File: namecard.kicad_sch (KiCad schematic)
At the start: 25 parts, among them J1 Conn_01x24, J2 Conn_01x05, Q1 AO3400A, U1 STM32G030K6Tx, U2 ST25DV04K-IER8C3

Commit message: 電源回路周りの調整
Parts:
- added C13, C8: 0.1uF, Capacitor_SMD:C_0603_1608Metric, symbol Device:C
- added D4: D_Schottky, symbol Device:D_Schottky
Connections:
- net +3.3V is gone; now on net EXT_3V3: C1.1, C4.1, L1.2
- net SYS_VDD is gone; now on net EXT_3V3: U1.4 (VDD)
- net EXT_3V3: now also U2.8 (VCC), C8.1, D4.1 (K)
- net GND: now also C13.2, C8.2
- net NRST: now also C13.1
- net V_EH_RAW: now also C_Tank1.1, D4.2 (A)

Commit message: 基盤配置の調整
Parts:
- removed C_Tank1: 330uF, Capacitor_Tantalum_SMD:CP_EIA-3216-18_Kemet-A, symbol Device:C
- added C14, C15, C16, C17, C18, C19, C20, C21, C22, C23: 22uf, Capacitor_SMD:C_0805_2012Metric, symbol Device:C
- D4: footprint (none) -> Diode_SMD:D_SOD-123
- J1: footprint Connector_FFC-FPC:Hirose_FH12-24S-0.5SH_1x24-1MP_P0.50mm_Horizontal -> FH34SRJ-24S-0.5SH(50)
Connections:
- net GND: now also C14.2, C15.2, C16.2, C17.2, C18.2, C19.2, C20.2, C21.2, C22.2, C23.2
- net V_EH_RAW: now also C14.1, C15.1, C16.1, C17.1, C18.1, C19.1, C20.1, C21.1, C22.1, C23.1

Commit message: v2 production
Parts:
- C14, C15, C16, C17, C18, C19, C20, C21, C22, C23: LCSC (none) -> C45783
- D4: LCSC (none) -> C22374920
- J1: footprint FH34SRJ-24S-0.5SH(50) -> Connector:FFC-SMD_24P-P0.50_FH34SRJ-24S-0.5SH; LCSC (none) -> C324726
- L1: LCSC (none) -> C66936
- U1: LCSC (none) -> C529331
- U2: LCSC (none) -> C2908287
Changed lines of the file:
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@@
 			)
 		)
+		(property "LCSC" "C45783"
+			(at 0 0 0)
+			(show_name no)
+			(do_not_autoplace no)
+			(effects
+				(font
+					(size 1.27 1.27)
+				)
+			)
+		)
 		(pin "1"
 		)
@@
 			)
 		)
+		(property "LCSC" "C22374920"
+			(at 35.56 66.04 0)
+			(hide yes)
+			(show_name no)
+			(do_not_autoplace no)
+			(effects
+				(font
+					(size 1.27 1.27)
+				)
+			)
+		)
 		(pin "1"
 		)
@@
 			)
 		)
+		(property "LCSC" "C66936"
+			(at 127 74.93 0)
+			(hide yes)
+			(show_name no)
+			(do_not_autoplace no)
+			(effects
+				(font
+					(size 1.27 1.27)
+				)
+			)
+		)
 		(pin "1"
 		)
@@
 			)
 		)
+		(property "LCSC" "C45783"
+			(at 0 0 0)
+			(show_name no)
+			(do_not_autoplace no)
+			(effects
+				(font
+					(size 1.27 1.27)
+				)
+			)
+		)
 		(pin "1"
 		)
@@
 			)
 		)
+		(property "LCSC" "C2908287"
+			(at 104.14 124.46 0)
+			(hide yes)
+			(show_name no)
+			(do_not_autoplace no)
+			(effects
+				(font
+					(size 1.27 1.27)
+				)
+			)
+		)
 		(pin "5"
 		)
@@
 			)
 		)
+		(property "LCSC" "C529331"
+			(at 44.45 115.57 0)
+			(hide yes)
+			(show_name no)
+			(do_not_autoplace no)
+			(effects
+				(font
+					(size 1.27 1.27)
+				)
+			)
+		)
 		(pin "20"
 		)
@@
 			)
 		)
+		(property "LCSC" "C45783"
+			(at 0 0 0)
+			(show_name no)
+			(do_not_autoplace no)
+			(effects
+				(font
+					(size 1.27 1.27)
+				)
+			)
+		)
 		(pin "1"
 		)
@@
 			)
 		)
+		(property "LCSC" "C45783"
+			(at 0 0 0)
+			(show_name no)
+			(do_not_autoplace no)
+			(effects
+				(font
+					(size 1.27 1.27)
+				)
+			)
+		)
 		(pin "1"
 		)
@@
 			)
 		)
+		(property "LCSC" "C45783"
+			(at 81.28 53.34 0)
+			(hide yes)
+			(show_name no)
+			(do_not_autoplace no)
+			(effects
+				(font
+					(size 1.27 1.27)
+				)
+			)
+		)
 		(pin "1"
 		)
@@
 			)
 		)
+		(property "LCSC" "C45783"
+			(at 0 0 0)
+			(show_name no)
+			(do_not_autoplace no)
+			(effects
+				(font
+					(size 1.27 1.27)
+				)
+			)
+		)
 		(pin "1"
 		)
@@
 			)
 		)
+		(property "LCSC" "C45783"
+			(at 0 0 0)
+			(show_name no)
+			(do_not_autoplace no)
+			(effects
+				(font
+					(size 1.27 1.27)
+				)
+			)
+		)
 		(pin "1"
 		)
@@
 			)
 		)
+		(property "LCSC" "C45783"
+			(at 0 0 0)
+			(show_name no)
+			(do_not_autoplace no)
+			(effects
+				(font
+					(size 1.27 1.27)
+				)
+			)
+		)
 		(pin "1"
 		)
@@
 			)
 		)
-		(property "Footprint" "FH34SRJ-24S-0.5SH(50)"
+		(property "Footprint" "Connector:FFC-SMD_24P-P0.50_FH34SRJ-24S-0.5SH"
 			(at 210.82 102.87 0)
 			(hide yes)
@@
 			)
 		)
+		(property "LCSC" "C324726"
+			(at 210.82 102.87 0)
+			(hide yes)
+			(show_name no)
+			(do_not_autoplace no)
+			(effects
+				(font
+					(size 1.27 1.27)
+				)
+			)
+		)
 		(pin "1"
 		)
@@
 			)
 		)
+		(property "LCSC" "C45783"
+			(at 0 0 0)
+			(show_name no)
+			(do_not_autoplace no)
+			(effects
+				(font
+					(size 1.27 1.27)
+				)
+			)
+		)
 		(pin "1"
 		)
@@
 			(show_name no)
 			(do_not_autoplace no)
+			(effects
+				(font
+					(size 1.27 1.27)
+				)
+			)
+		)
+		(property "LCSC" "C45783"
+			(at 0 0 0)
+			(show_name no)
+			(do_not_autoplace no)

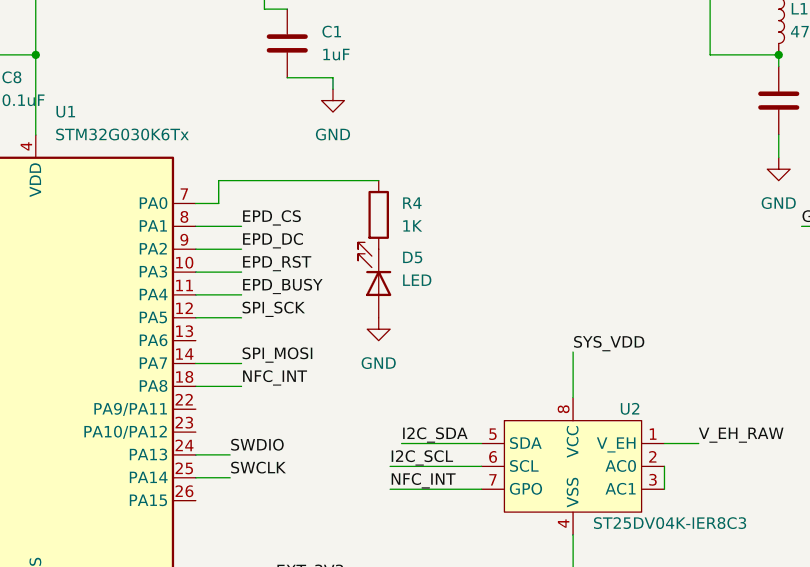
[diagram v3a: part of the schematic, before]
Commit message: V3向けの変更:LEDの向きを直したり
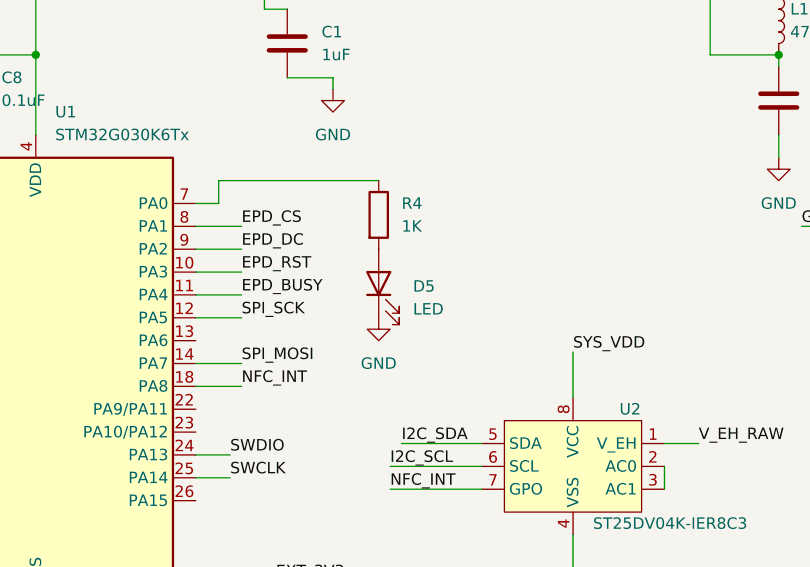
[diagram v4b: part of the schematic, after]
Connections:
- net GND: now also D5.1 (K); no longer D5.2 (A)
- net at R4.2: now also D5.2 (A); no longer D5.1 (K)
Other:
- moved on the sheet: D5
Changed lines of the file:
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@@
 	(symbol
 		(lib_id "Device:LED")
-		(at 82.55 104.14 270)
+		(at 82.55 104.14 90)
 		(unit 1)
 		(body_style 1)
@@
 		(fields_autoplaced yes)
 		(property "Reference" "D5"
-			(at 85.09 101.2824 90)
+			(at 86.36 104.4574 90)
 			(show_name no)
 			(do_not_autoplace no)
@@
 					(size 1.27 1.27)
 				)
-				(justify left)
+				(justify right)
 			)
 		)
 		(property "Value" "LED"
-			(at 85.09 103.8224 90)
+			(at 86.36 106.9974 90)
 			(show_name no)
 			(do_not_autoplace no)
@@
 					(size 1.27 1.27)
 				)
-				(justify left)
+				(justify right)
 			)
 		)

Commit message: v3
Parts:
- removed C19, C20, C21, C22: 22uf, Capacitor_SMD:C_0805_2012Metric, symbol Device:C
- removed D5: LED, LED_SMD:LED_0603_1608Metric, symbol Device:LED
- added R3: 1M, Resistor_SMD:R_0603_1608Metric, symbol Device:R
- added R5: 470k, Resistor_SMD:R_0603_1608Metric, symbol Device:R
- added TP1, TP3, TP4, TP5, TP6, TP7: TestPoint, TestPoint:TestPoint_Pad_D1.0mm, symbol Connector:TestPoint
- added U3: TPS22917DBV, Package_TO_SOT_SMD:SOT-23-6, symbol Power_Management:TPS22917DBV
- C14, C15, C16, C17: value 22uf -> 220uf; footprint Capacitor_SMD:C_0805_2012Metric -> Capacitor_Tantalum_SMD:6TPE220MAZB; JLCPCB (none) -> C79111; LCSC C45783 -> (none)
- C18: value 22uf -> 100nf; footprint Capacitor_SMD:C_0805_2012Metric -> Capacitor_SMD:C_0603_1608Metric; LCSC C45783 -> (none)
- C23: JLCPCB (none) -> C45783; LCSC C45783 -> (none)
- D4: footprint Diode_SMD:D_SOD-123 -> Diode_SMD:D_SOD-123F; JLCPCB (none) -> C110921; LCSC C22374920 -> (none)
- J1: footprint Connector:FFC-SMD_24P-P0.50_FH34SRJ-24S-0.5SH -> Connector_FFC-FPC:Hirose_FH12-24S-0.5SH_1x24-1MP_P0.50mm_Horizontal; JLCPCB (none) -> C506794; LCSC C324726 -> (none)
- L1: JLCPCB (none) -> C66936; LCSC C66936 -> (none)
- R4: value 1K -> 100k
- U1: JLCPCB (none) -> C529331; LCSC C529331 -> (none)
- U2: JLCPCB (none) -> C2908287; LCSC C2908287 -> (none)
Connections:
- net EPD_BUSY: now also J1.16 (Pin_16); no longer J1.9 (Pin_9)
- net EPD_CS: now also J1.13 (Pin_13); no longer J1.12 (Pin_12)
- net EPD_DC: now also J1.14 (Pin_14); no longer J1.11 (Pin_11)
- net EPD_RST: now also J1.15 (Pin_15); no longer J1.10 (Pin_10)
- net EXT_3V3: now also C14.1, C15.1, C16.1, C17.1, R3.1, TP1.1, U3.1 (VIN)
- net GDR: now also J1.23 (Pin_23); no longer J1.2 (Pin_2)
- net GND: now also C11.2, C18.1, J1.20 (Pin_20), R4.2, R5.2, TP7.1; no longer C11.1, C18.2, J1.17 (Pin_17)
- net PREVGH: now also J1.4 (Pin_4); no longer J1.21 (Pin_21)
- net PREVGL: now also C11.1, J1.2 (Pin_2); no longer C11.2, J1.23 (Pin_23)
- net RESE: now also J1.22 (Pin_22); no longer J1.3 (Pin_3)
- net SPI_MOSI: now also J1.11 (Pin_11); no longer J1.14 (Pin_14)
- net SPI_SCK: now also J1.12 (Pin_12); no longer J1.13 (Pin_13)
- net V_EH_RAW: now also TP3.1; no longer C14.1, C15.1, C16.1, C17.1, C18.1
- net at C7.1: now also J1.5 (Pin_5); no longer J1.18 (Pin_18)
- net at U1.13 (PA6): now also U3.3 (ON)
- net at U1.22 (PA9/PA11): now also TP4.1
- net at U1.23 (PA10/PA12): now also TP5.1
- net at R4.1: now also U3.4 (CT); no longer U1.7 (PA0)
- net at C12.2: now also J1.1 (Pin_1); no longer J1.24 (Pin_24)
- net EPD_SW: now reaches C9.1
- net EPD_SW: now also C18.2, J1.10 (Pin_10), J1.9 (Pin_9), TP6.1, U3.6 (VOUT); no longer J1.20 (Pin_20)
- net at C2.1: now also J1.17 (Pin_17); no longer J1.5 (Pin_5)
- net at C10.1: now also J1.3 (Pin_3); no longer J1.22 (Pin_22)
- net at J1.7 (Pin_7): now also C6.1
- new net: R3.2, R5.1, U1.7 (PA0)
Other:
- moved on the sheet: C1, C10, C11, C12, C2, C23, C6, C7, C9, D4, J1, U2

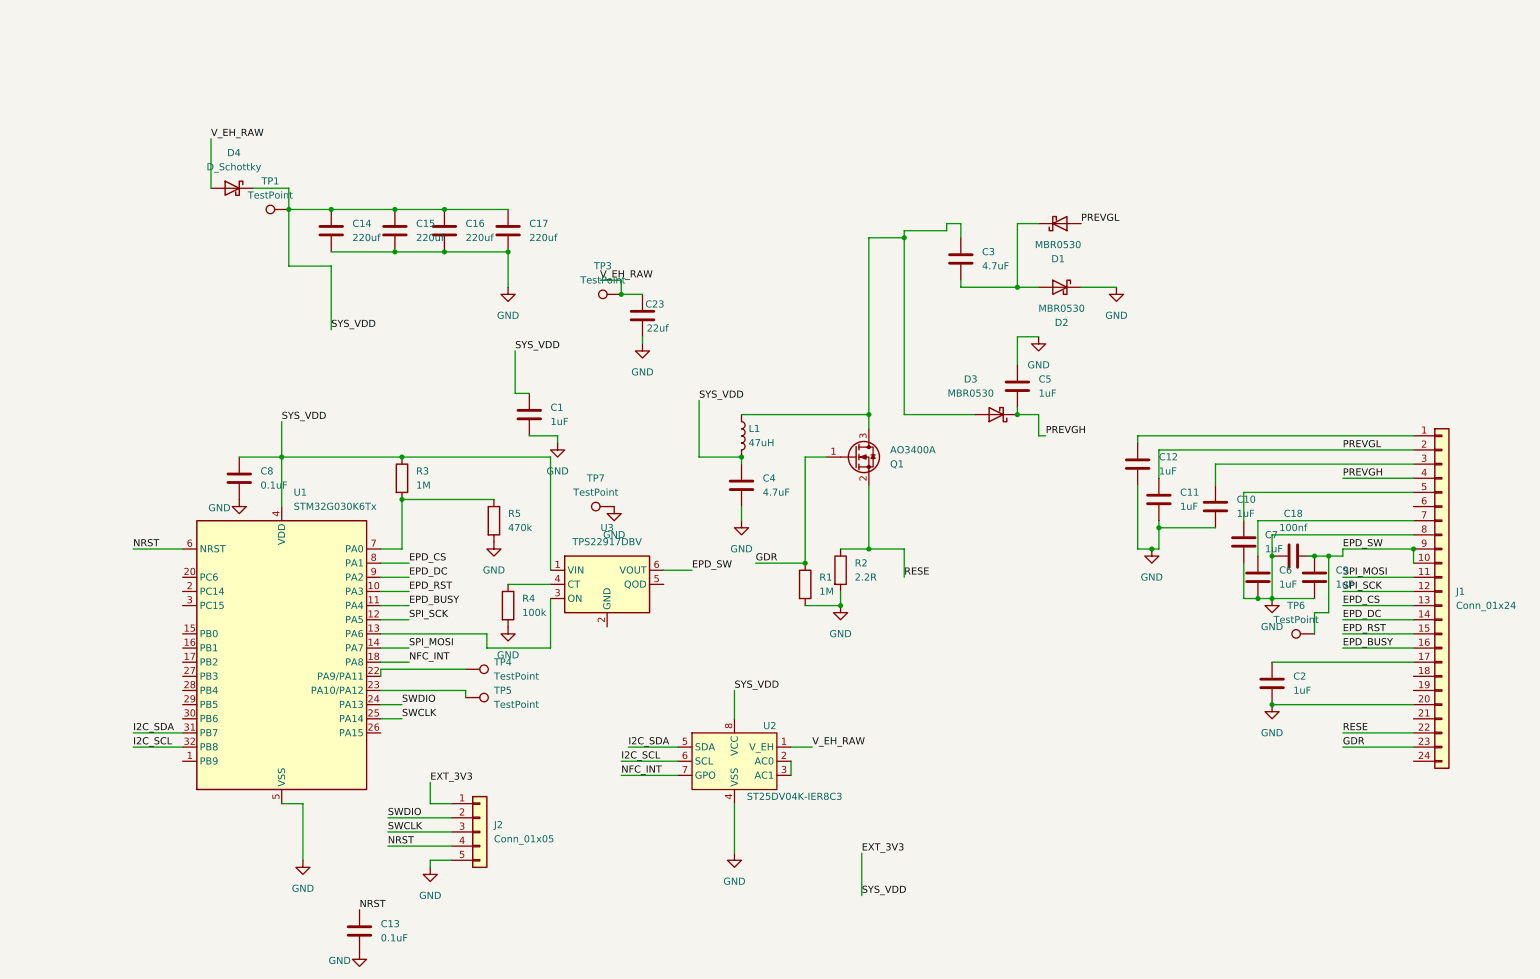
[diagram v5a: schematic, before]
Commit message: wip: 電源周りの回路図を更新
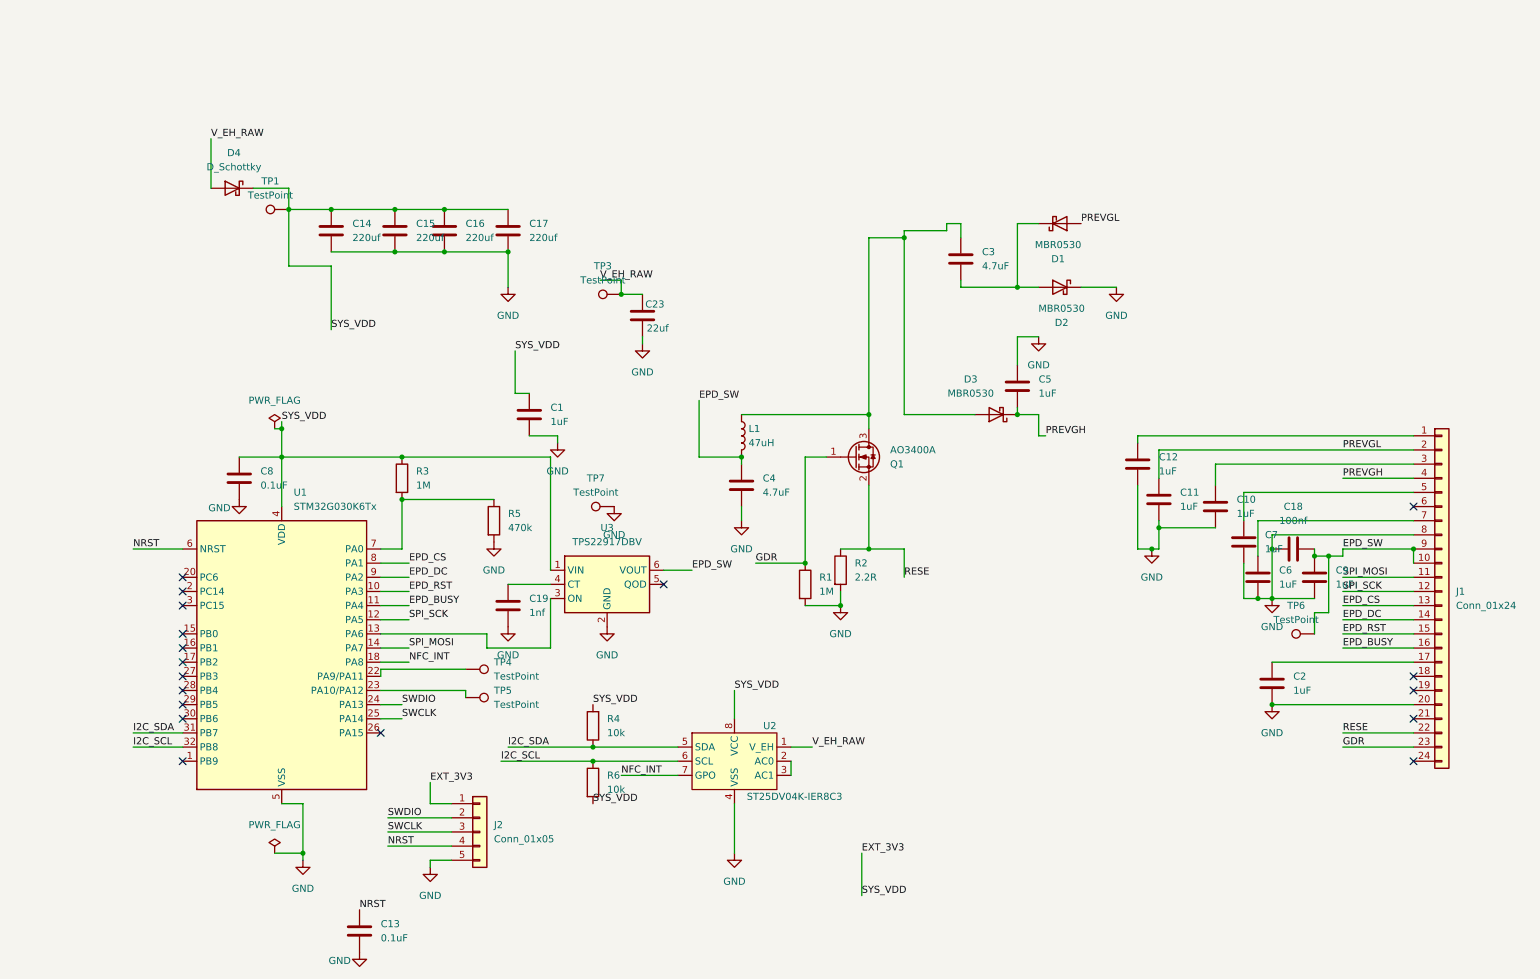
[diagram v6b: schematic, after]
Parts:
- added C19: 1nf, Capacitor_SMD:C_0603_1608Metric, symbol Device:C
- added R6: 10k, Resistor_SMD:R_0603_1608Metric, symbol Device:R
- R4: value 100k -> 10k
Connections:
- net EPD_SW: now also C4.1, L1.2
- net EXT_3V3: now also R4.2, R6.2; no longer C4.1, L1.2
- net GND: now also U3.2 (GND), C19.2; no longer R4.2
- net I2C_SCL: now also R6.1
- net I2C_SDA: now also R4.1
- net at U3.4 (CT): now also C19.1; no longer R4.1
- no-connect marks 0 -> 18
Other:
- moved on the sheet: C18

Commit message: wip: 配置を更新
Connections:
- net EXT_3V3 renamed SYS_VDD
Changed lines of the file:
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@@
-	(wire
-		(pts
-			(xy 148.59 149.86) (xy 148.59 157.48)
-		)
-		(stroke
-			(width 0)
-			(type default)
-		)
-	)
 	(wire
 		(pts
@@
 		)
 	)
-	(label "EXT_3V3"
+	(label "SYS_VDD"
 		(at 71.12 137.16 0)
 		(effects
@@
 		)
 	)
-	(label "EXT_3V3"
-		(at 148.59 149.86 0)
-		(effects
-			(font
-				(size 1.27 1.27)
-			)
-			(justify left bottom)
-		)
-	)
 	(label "SPI_MOSI"
 		(at 234.95 100.33 0)
@@
 		(effects
 			(font
-				(size 1.27 1.27)
-			)
-			(justify left bottom)
-		)
-	)
-	(label "SYS_VDD"
-		(at 148.59 157.48 0)
-		(effects
-			(font
